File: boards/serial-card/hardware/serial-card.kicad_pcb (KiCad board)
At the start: 2 copper layers, 100 x 100 mm, 4 parts

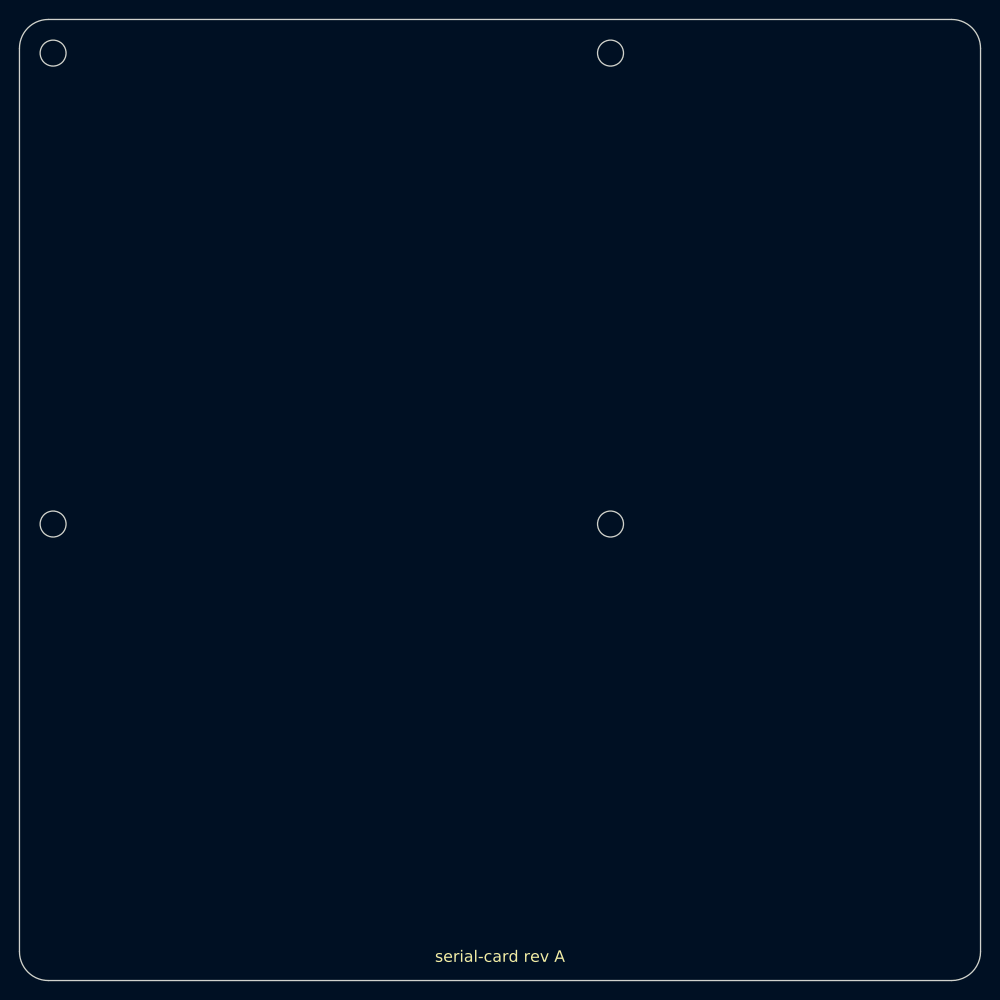
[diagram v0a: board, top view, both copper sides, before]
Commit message: serial-card: placed + routed (check_board clean); duplex survey in README
Survey: Magna-Power, B&K 1696-98, Mean Well Modbus RTU and the ITECH/Maynuo
RS-485 converters are 2-wire half duplex; TDK-Lambda Genesys is 4-wire but
its first unit also takes RS-232, so half duplex stays. Floorplan: LOGIC
left (J20 top edge, J21 bottom edge), RS485_3/4 top/bottom right with the
ISOW1432 on the 2 mm gap and headers on the right edge, no copper around
J11 (rack 12 V pass-through), TI 4 mm keep-outs. place.py / route.py.

Co-Authored-By: Claude Opus 5.5 <noreply@anthropic.com>
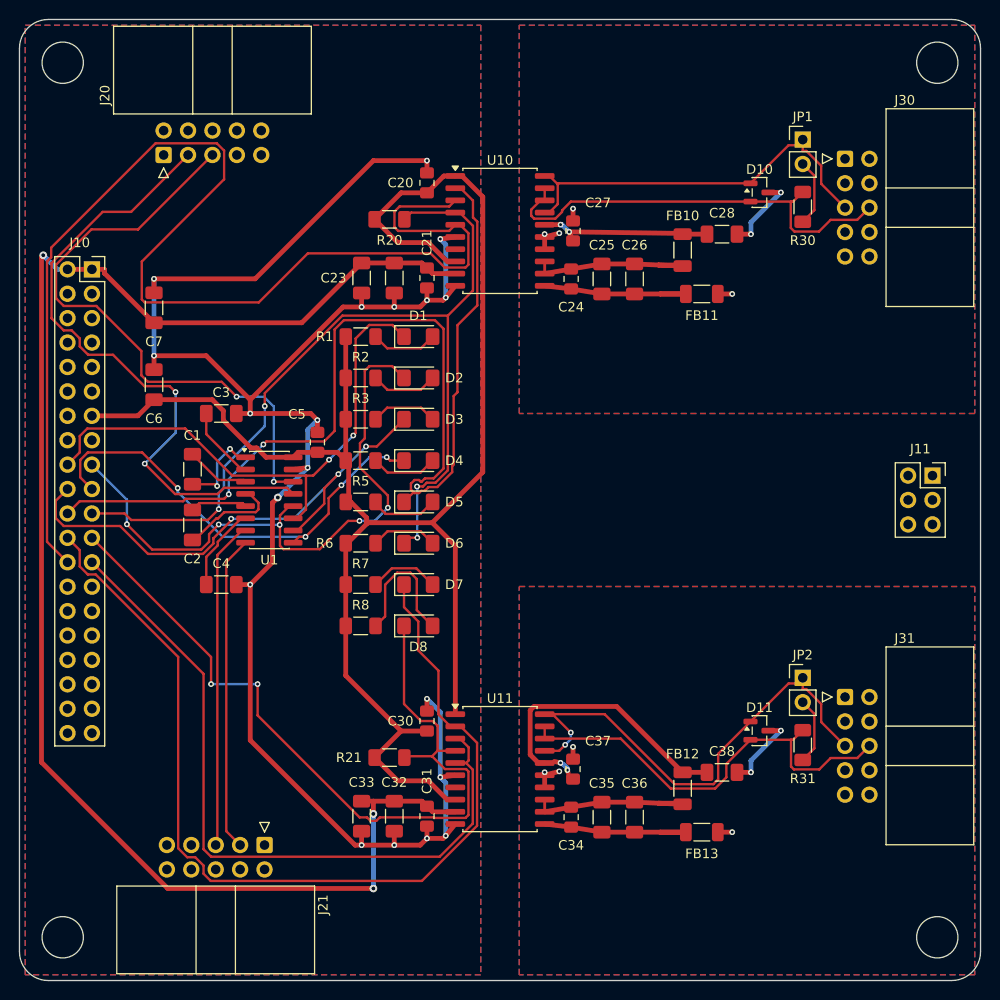
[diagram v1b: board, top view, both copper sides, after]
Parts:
- added C1: 100nF 50V X7R, Capacitor_SMD:C_1206_3216Metric_Pad1.33x1.80mm_HandSolder, F.Cu at (118.0, 146.8)
- added C2: 100nF 50V X7R, Capacitor_SMD:C_1206_3216Metric_Pad1.33x1.80mm_HandSolder, F.Cu at (118.0, 152.6)
- added C20: 100nF 50V X7R, Capacitor_SMD:C_0805_2012Metric_Pad1.18x1.45mm_HandSolder, F.Cu at (142.4, 117.0)
- added C21: 10nF 50V X7R, Capacitor_SMD:C_0805_2012Metric_Pad1.18x1.45mm_HandSolder, F.Cu at (142.4, 126.9)
- added C22: 1uF 50V X7R, Capacitor_SMD:C_1206_3216Metric_Pad1.33x1.80mm_HandSolder, F.Cu at (139.0, 126.9)
- added C23: 10uF 25V X7R, Capacitor_SMD:C_1206_3216Metric_Pad1.33x1.80mm_HandSolder, F.Cu at (135.6, 126.9)
- added C24: 10nF 50V X7R, Capacitor_SMD:C_0805_2012Metric_Pad1.18x1.45mm_HandSolder, F.Cu at (157.4, 127.0)
- added C25: 1uF 50V X7R, Capacitor_SMD:C_1206_3216Metric_Pad1.33x1.80mm_HandSolder, F.Cu at (160.6, 127.0)
- added C26: 10uF 25V X7R, Capacitor_SMD:C_1206_3216Metric_Pad1.33x1.80mm_HandSolder, F.Cu at (164.0, 127.0)
- added C27: 100nF 50V X7R, Capacitor_SMD:C_0805_2012Metric_Pad1.18x1.45mm_HandSolder, F.Cu at (157.6, 122.0)
- added C28: 10uF 25V X7R, Capacitor_SMD:C_1206_3216Metric_Pad1.33x1.80mm_HandSolder, F.Cu at (173.1, 122.3)
- added C3: 100nF 50V X7R, Capacitor_SMD:C_1206_3216Metric_Pad1.33x1.80mm_HandSolder, F.Cu at (121.0, 141.0)
- added C30: 100nF 50V X7R, Capacitor_SMD:C_0805_2012Metric_Pad1.18x1.45mm_HandSolder, F.Cu at (142.4, 173.0)
- added C31: 10nF 50V X7R, Capacitor_SMD:C_0805_2012Metric_Pad1.18x1.45mm_HandSolder, F.Cu at (142.4, 182.9)
- added C32: 1uF 50V X7R, Capacitor_SMD:C_1206_3216Metric_Pad1.33x1.80mm_HandSolder, F.Cu at (139.0, 182.9)
- added C33: 10uF 25V X7R, Capacitor_SMD:C_1206_3216Metric_Pad1.33x1.80mm_HandSolder, F.Cu at (135.6, 182.9)
- added C34: 10nF 50V X7R, Capacitor_SMD:C_0805_2012Metric_Pad1.18x1.45mm_HandSolder, F.Cu at (157.4, 183.0)
- added C35: 1uF 50V X7R, Capacitor_SMD:C_1206_3216Metric_Pad1.33x1.80mm_HandSolder, F.Cu at (160.6, 183.0)
- added C36: 10uF 25V X7R, Capacitor_SMD:C_1206_3216Metric_Pad1.33x1.80mm_HandSolder, F.Cu at (164.0, 183.0)
- added C37: 100nF 50V X7R, Capacitor_SMD:C_0805_2012Metric_Pad1.18x1.45mm_HandSolder, F.Cu at (157.6, 178.0)
- added C38: 10uF 25V X7R, Capacitor_SMD:C_1206_3216Metric_Pad1.33x1.80mm_HandSolder, F.Cu at (173.1, 178.3)
- added C4: 100nF 50V X7R, Capacitor_SMD:C_1206_3216Metric_Pad1.33x1.80mm_HandSolder, F.Cu at (121.0, 158.8)
- added C5: 100nF 50V X7R, Capacitor_SMD:C_0805_2012Metric_Pad1.18x1.45mm_HandSolder, F.Cu at (131.0, 144.0)
- added C6: 10uF 25V X7R, Capacitor_SMD:C_1206_3216Metric_Pad1.33x1.80mm_HandSolder, F.Cu at (114.0, 138.0)
- added C7: 10uF 25V X7R, Capacitor_SMD:C_1206_3216Metric_Pad1.33x1.80mm_HandSolder, F.Cu at (114.0, 130.0)
- added D1: LED green, LED_SMD:LED_1206_3216Metric_Pad1.42x1.75mm_HandSolder, F.Cu at (141.5, 133.0)
- added D10: SM712, Package_TO_SOT_SMD:SOT-23, F.Cu at (177.0, 118.0)
- added D11: SM712, Package_TO_SOT_SMD:SOT-23, F.Cu at (177.0, 174.0)
- added D2: LED yellow, LED_SMD:LED_1206_3216Metric_Pad1.42x1.75mm_HandSolder, F.Cu at (141.5, 137.3)
- added D3: LED green, LED_SMD:LED_1206_3216Metric_Pad1.42x1.75mm_HandSolder, F.Cu at (141.5, 141.6)
- added D4: LED yellow, LED_SMD:LED_1206_3216Metric_Pad1.42x1.75mm_HandSolder, F.Cu at (141.5, 145.9)
- added D5: LED green, LED_SMD:LED_1206_3216Metric_Pad1.42x1.75mm_HandSolder, F.Cu at (141.5, 150.2)
- added D6: LED yellow, LED_SMD:LED_1206_3216Metric_Pad1.42x1.75mm_HandSolder, F.Cu at (141.5, 154.5)
- added D7: LED green, LED_SMD:LED_1206_3216Metric_Pad1.42x1.75mm_HandSolder, F.Cu at (141.5, 158.8)
- added D8: LED yellow, LED_SMD:LED_1206_3216Metric_Pad1.42x1.75mm_HandSolder, F.Cu at (141.5, 163.1)
- added FB10: BLM31KN102SN1L, Inductor_SMD:L_1206_3216Metric_Pad1.22x1.90mm_HandSolder, F.Cu at (169.0, 124.0)
- added FB11: BLM31KN102SN1L, Inductor_SMD:L_1206_3216Metric_Pad1.22x1.90mm_HandSolder, F.Cu at (171.0, 128.6)
- added FB12: BLM31KN102SN1L, Inductor_SMD:L_1206_3216Metric_Pad1.22x1.90mm_HandSolder, F.Cu at (169.0, 180.0)
- added FB13: BLM31KN102SN1L, Inductor_SMD:L_1206_3216Metric_Pad1.22x1.90mm_HandSolder, F.Cu at (171.0, 184.6)
- added J10: STACK BUS, Connector_PinSocket_2.54mm:PinSocket_2x20_P2.54mm_Vertical, F.Cu at (107.5, 126.0)
- added J11: RACK 12V, Connector_PinSocket_2.54mm:PinSocket_2x03_P2.54mm_Vertical, F.Cu at (195.0, 147.5)
- added J20: RS-232 1, Connector_IDC:IDC-Header_2x05_P2.54mm_Horizontal, F.Cu at (115.0, 114.1)
- added J21: RS-232 2, Connector_IDC:IDC-Header_2x05_P2.54mm_Horizontal, F.Cu at (125.5, 185.9)
- added J30: RS-485 3, Connector_IDC:IDC-Header_2x05_P2.54mm_Horizontal, F.Cu at (185.9, 114.5)
- added J31: RS-485 4, Connector_IDC:IDC-Header_2x05_P2.54mm_Horizontal, F.Cu at (185.9, 170.5)
- added JP1: TERM, Connector_PinHeader_2.54mm:PinHeader_1x02_P2.54mm_Vertical, F.Cu at (181.5, 112.5)
- added JP2: TERM, Connector_PinHeader_2.54mm:PinHeader_1x02_P2.54mm_Vertical, F.Cu at (181.5, 168.5)
- added R1: 1k, Resistor_SMD:R_1206_3216Metric_Pad1.30x1.75mm_HandSolder, F.Cu at (135.5, 133.0)
- added R2: 1k, Resistor_SMD:R_1206_3216Metric_Pad1.30x1.75mm_HandSolder, F.Cu at (135.5, 137.3)
- added R20: 10k, Resistor_SMD:R_1206_3216Metric_Pad1.30x1.75mm_HandSolder, F.Cu at (138.5, 120.8)
- added R21: 10k, Resistor_SMD:R_1206_3216Metric_Pad1.30x1.75mm_HandSolder, F.Cu at (138.5, 176.8)
- added R3: 1k, Resistor_SMD:R_1206_3216Metric_Pad1.30x1.75mm_HandSolder, F.Cu at (135.5, 141.6)
- added R30: 120R, Resistor_SMD:R_1206_3216Metric_Pad1.30x1.75mm_HandSolder, F.Cu at (181.5, 119.5)
- added R31: 120R, Resistor_SMD:R_1206_3216Metric_Pad1.30x1.75mm_HandSolder, F.Cu at (181.5, 175.5)
- added R4: 1k, Resistor_SMD:R_1206_3216Metric_Pad1.30x1.75mm_HandSolder, F.Cu at (135.5, 145.9)
- added R5: 1k, Resistor_SMD:R_1206_3216Metric_Pad1.30x1.75mm_HandSolder, F.Cu at (135.5, 150.2)
- added R6: 1k, Resistor_SMD:R_1206_3216Metric_Pad1.30x1.75mm_HandSolder, F.Cu at (135.5, 154.5)
- added R7: 1k, Resistor_SMD:R_1206_3216Metric_Pad1.30x1.75mm_HandSolder, F.Cu at (135.5, 158.8)
- added R8: 1k, Resistor_SMD:R_1206_3216Metric_Pad1.30x1.75mm_HandSolder, F.Cu at (135.5, 163.1)
- added U1: ST3232B, Package_SO:SOIC-16_3.9x9.9mm_P1.27mm, F.Cu at (126.0, 150.0)
- added U10: ISOW1432, Package_SO:SOIC-20W_7.5x12.8mm_P1.27mm, F.Cu at (150.0, 122.0)
- added U11: ISOW1432, Package_SO:SOIC-20W_7.5x12.8mm_P1.27mm, F.Cu at (150.0, 178.0)
- MH1, MH2, MH3, MH4: value MountingHole_2.7mm_M2.5 -> MountingHole_4.3mm_M4_Standoff7mm; footprint MountingHole:MountingHole_2.7mm_M2.5 -> Thl_Mechanical:MountingHole_4.3mm_M4_Standoff7mm
- moved MH4 54.8 mm to (195.5, 195.5)
- moved MH3 43.0 mm to (104.5, 195.5)
- moved MH2 34.0 mm to (195.5, 104.5)
- moved MH1 1.41 mm to (104.5, 104.5)
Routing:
- net GND: track 0.00 -> 195.5 mm, vias 0 -> 19
- net +3V3: track 0.00 -> 181.5 mm
- net +5V: track 0.00 -> 161.2 mm, vias 0 -> 3
- net /DE1: track 0.00 -> 132.8 mm
- net /U4TX: track 0.00 -> 112.9 mm, vias 0 -> 2
- net /U5TX: track 0.00 -> 101.8 mm
- net /U4RX: track 0.00 -> 95.8 mm, vias 0 -> 4
- net /U5RX: track 0.00 -> 85.0 mm, vias 0 -> 2
- net /DE2: track 0.00 -> 75.6 mm
- net /RXD1: track 0.00 -> 67.2 mm, vias 0 -> 2
- net /U2RX: track 0.00 -> 64.8 mm, vias 0 -> 5
- net /TXD1: track 0.00 -> 63.1 mm, vias 0 -> 2
- net /U2TX: track 0.00 -> 57.6 mm, vias 0 -> 2
- net /U3TX: track 0.00 -> 55.6 mm, vias 0 -> 3
- net /DP4: track 0.00 -> 52.3 mm, vias 0 -> 2
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- added copper zone on B.Cu, net /GND_485_3
- added copper zone on F.Cu, net /GND_485_3
- added copper zone on B.Cu, net /GND_485_4
- added copper zone on F.Cu, net /GND_485_4
- added copper zone on B.Cu, net GND
- added copper zone on F.Cu, net GND
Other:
- board text removed: "serial-card rev ${REVISION}"

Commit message: Probe test points on all fab boards; golden-board R/C/L test tool
tools/testpoints.py puts a 1.0 mm bare-copper pad (Thl_TestPoint:
TP_Probe_D1.0mm, board-only, no silkscreen) on every net of core,
can-card, io-card, serial-card and can-ssr, only on copper the net
already has (track, via or pour): no routing changes. Clear of foreign
copper, courtyards, all silkscreen, isolation gaps; 0.5 mm from the net's
own pads so the probe measures through the joint. Where nothing fits the
probe point is an SMD pad toe. Bottom-side test points where the parts
are on the bottom (can-ssr). DRC loop moves offenders; check_board clean
on all five boards, no reference texts moved or hidden.

tools/tptest.py: plan (net vs domain ground, across two-pin parts,
isolation between ground domains; powered.csv rail checklist) and run
(golden recording, compare with tolerance + golden spread, serial stream
from the planned probe helper or typed values, current.png step map).
docs/probe-test.md describes the workflow and the helper's interface.

Also: silk_tidy --only and board.json silk_keep; io-card place.py places
the AO row references; place.py scripts ignore TP footprints.

Co-Authored-By: Claude Opus 5.5 <noreply@anthropic.com>
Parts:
- added TP1: pour, Thl_TestPoint:TP_Probe_D1.0mm, F.Cu at (147.6, 101.6)
- added TP10: track, Thl_TestPoint:TP_Probe_D1.0mm, F.Cu at (110.0, 135.2)
- added TP11: track, Thl_TestPoint:TP_Probe_D1.0mm, F.Cu at (119.4, 137.7)
- added TP12: track, Thl_TestPoint:TP_Probe_D1.0mm, F.Cu at (129.4, 131.6)
- added TP13: track, Thl_TestPoint:TP_Probe_D1.0mm, F.Cu at (110.0, 145.1)
- added TP14: track, Thl_TestPoint:TP_Probe_D1.0mm, F.Cu at (115.5, 142.6)
- added TP15: track, Thl_TestPoint:TP_Probe_D1.0mm, F.Cu at (119.6, 143.3)
- added TP16: track, Thl_TestPoint:TP_Probe_D1.0mm, F.Cu at (119.9, 147.1)
- added TP17: track, Thl_TestPoint:TP_Probe_D1.0mm, F.Cu at (122.7, 143.1)
- added TP18: track, Thl_TestPoint:TP_Probe_D1.0mm, F.Cu at (138.1, 143.5)
- added TP19: pour, Thl_TestPoint:TP_Probe_D1.0mm, F.Cu at (198.5, 140.6)
- added TP2: pour, Thl_TestPoint:TP_Probe_D1.0mm, F.Cu at (152.5, 101.6)
- added TP20: track, Thl_TestPoint:TP_Probe_D1.0mm, F.Cu at (115.0, 150.1)
- added TP21: track, Thl_TestPoint:TP_Probe_D1.0mm, F.Cu at (116.1, 152.1)
- added TP22: track, Thl_TestPoint:TP_Probe_D1.0mm, F.Cu at (134.0, 152.3)
- added TP23: track, Thl_TestPoint:TP_Probe_D1.0mm, F.Cu at (117.9, 166.8)
- added TP24: track, Thl_TestPoint:TP_Probe_D1.0mm, F.Cu at (120.6, 162.5)
- added TP25: track, Thl_TestPoint:TP_Probe_D1.0mm, F.Cu at (121.5, 160.8)
- added TP26: track, Thl_TestPoint:TP_Probe_D1.0mm, F.Cu at (138.0, 160.8)
- added TP27: pour, Thl_TestPoint:TP_Probe_D1.0mm, F.Cu at (101.6, 178.6)
- added TP28: track, Thl_TestPoint:TP_Probe_D1.0mm, F.Cu at (143.1, 176.8)
- added TP29: track, Thl_TestPoint:TP_Probe_D1.0mm, F.Cu at (162.1, 171.5)
- added TP3: track, Thl_TestPoint:TP_Probe_D1.0mm, F.Cu at (111.0, 116.1)
- added TP30: track, Thl_TestPoint:TP_Probe_D1.0mm, F.Cu at (179.0, 170.1)
- added TP31: track, Thl_TestPoint:TP_Probe_D1.0mm, F.Cu at (183.8, 177.4)
- added TP32: track, Thl_TestPoint:TP_Probe_D1.0mm, F.Cu at (143.0, 188.5)
- added TP33: track, Thl_TestPoint:TP_Probe_D1.0mm, F.Cu at (166.5, 181.6)
- added TP34: track, Thl_TestPoint:TP_Probe_D1.0mm, F.Cu at (166.7, 184.6)
- added TP35: pour, Thl_TestPoint:TP_Probe_D1.0mm, F.Cu at (147.6, 198.6)
- added TP36: pour, Thl_TestPoint:TP_Probe_D1.0mm, F.Cu at (198.5, 191.5)
- added TP4: track, Thl_TestPoint:TP_Probe_D1.0mm, F.Cu at (174.3, 117.0)
- added TP5: track, Thl_TestPoint:TP_Probe_D1.0mm, F.Cu at (115.6, 127.0)
- added TP6: track, Thl_TestPoint:TP_Probe_D1.0mm, F.Cu at (159.3, 122.1)
- added TP7: track, Thl_TestPoint:TP_Probe_D1.0mm, F.Cu at (166.0, 125.5)
- added TP8: track, Thl_TestPoint:TP_Probe_D1.0mm, F.Cu at (166.7, 128.6)
- added TP9: track, Thl_TestPoint:TP_Probe_D1.0mm, F.Cu at (183.8, 121.4)

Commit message: Rev A order files; serial-card box headers checked against the vendor model
docs/orders: DigiKey upload CSV for one set of the six boards to order
(core, can-card, io-card, serial-card, can-ssr, probe-helper: 121 lines,
450 parts) and a README listing the items not in the board BOMs
(mating plugs, shunts, cables, standoffs) plus the assembly note below.

serial-card J20/J21/J30/J31 use Thl_Connector:Amphenol_T821110A1R100CEU_
2x05_P2.54mm_Horizontal (stock IDC pads, which match Amphenol's land
pattern, plus the SamacSys STEP from transfer/, kept local per its
licence). The body is 8.86 mm (the stock model showed 11.1 mm), leaving
2.3 mm under the next board (ESQ-120-14, 11.18 mm); THT tails of the board
above land over the headers in every stack order, so tails under the
stack boards are trimmed to about 1.5 mm.

io-card README: AQW212 is the AC/DC type, so off outputs block a reversed
coil supply.

Co-Authored-By: Claude Opus 5.5 <noreply@anthropic.com>
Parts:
- J20, J21, J30, J31: footprint Connector_IDC:IDC-Header_2x05_P2.54mm_Horizontal -> Thl_Connector:Amphenol_T821110A1R100CEU_2x05_P2.54mm_Horizontal
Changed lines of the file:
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@@
 		)
 	)
-	(footprint "Connector_IDC:IDC-Header_2x05_P2.54mm_Horizontal"
+	(footprint "Thl_Connector:Amphenol_T821110A1R100CEU_2x05_P2.54mm_Horizontal"
 		(layer "F.Cu")
 		(at 125.5 185.9 -90)
@@
 		)
 		(embedded_fonts no)
-		(model "${KIPRJMOD}/../../../lib/3dmodels/Connector_IDC.3dshapes/IDC-Header_2x05_P2.54mm_Horizontal.step"
+		(model "${KIPRJMOD}/../../../lib/3dmodels/Thl_Connector.3dshapes/Amphenol_T821110A1R100CEU.step"
 			(offset
-				(xyz 0 0 0)
+				(xyz 4.24 -5.11 4.46)
 			)
 			(scale
@@
 			)
 			(rotate
-				(xyz 0 0 0)
+				(xyz 0 0 90)
 			)
 		)
@@
 		)
 	)
-	(footprint "Connector_IDC:IDC-Header_2x05_P2.54mm_Horizontal"
+	(footprint "Thl_Connector:Amphenol_T821110A1R100CEU_2x05_P2.54mm_Horizontal"
 		(layer "F.Cu")
 		(at 185.9 170.5)
@@
 		)
 		(embedded_fonts no)
-		(model "${KIPRJMOD}/../../../lib/3dmodels/Connector_IDC.3dshapes/IDC-Header_2x05_P2.54mm_Horizontal.step"
+		(model "${KIPRJMOD}/../../../lib/3dmodels/Thl_Connector.3dshapes/Amphenol_T821110A1R100CEU.step"
 			(offset
-				(xyz 0 0 0)
+				(xyz 4.24 -5.11 4.46)
 			)
 			(scale
@@
 			)
 			(rotate
-				(xyz 0 0 0)
+				(xyz 0 0 90)
 			)
 		)
@@
 		)
 	)
-	(footprint "Connector_IDC:IDC-Header_2x05_P2.54mm_Horizontal"
+	(footprint "Thl_Connector:Amphenol_T821110A1R100CEU_2x05_P2.54mm_Horizontal"
 		(layer "F.Cu")
 		(at 115 114.1 90)
@@
 		)
 		(embedded_fonts no)
-		(model "${KIPRJMOD}/../../../lib/3dmodels/Connector_IDC.3dshapes/IDC-Header_2x05_P2.54mm_Horizontal.step"
+		(model "${KIPRJMOD}/../../../lib/3dmodels/Thl_Connector.3dshapes/Amphenol_T821110A1R100CEU.step"
 			(offset
-				(xyz 0 0 0)
+				(xyz 4.24 -5.11 4.46)
 			)
 			(scale
@@
 			)
 			(rotate
-				(xyz 0 0 0)
+				(xyz 0 0 90)
 			)
 		)
@@
 		(embedded_fonts no)
 	)
-	(footprint "Connector_IDC:IDC-Header_2x05_P2.54mm_Horizontal"
+	(footprint "Thl_Connector:Amphenol_T821110A1R100CEU_2x05_P2.54mm_Horizontal"
 		(layer "F.Cu")
 		(at 185.9 114.5)
@@
 		)
 		(embedded_fonts no)
-		(model "${KIPRJMOD}/../../../lib/3dmodels/Connector_IDC.3dshapes/IDC-Header_2x05_P2.54mm_Horizontal.step"
+		(model "${KIPRJMOD}/../../../lib/3dmodels/Thl_Connector.3dshapes/Amphenol_T821110A1R100CEU.step"
 			(offset
-				(xyz 0 0 0)
+				(xyz 4.24 -5.11 4.46)
 			)
 			(scale
@@
 			)
 			(rotate
-				(xyz 0 0 0)
+				(xyz 0 0 90)
 			)
 		)
